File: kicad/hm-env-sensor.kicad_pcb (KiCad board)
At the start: 2 copper layers, 40 x 79 mm, 65 parts, among them Q1 Q12MHz/20pF/10ppm/4P/3.2x2.5mm, Q2 BC817-40(SOT23), Q3 BC817-40(SOT23), U1 BL4054B-42TPRN(SOT23-5), U2 CH340T(SSOP20W), U3 SY8089AAAC(SOT23-5), U4 BAT54C(SOT23-3), U5 ESP-WROOM-32, U6 BQ27441-G1, U7 BME280

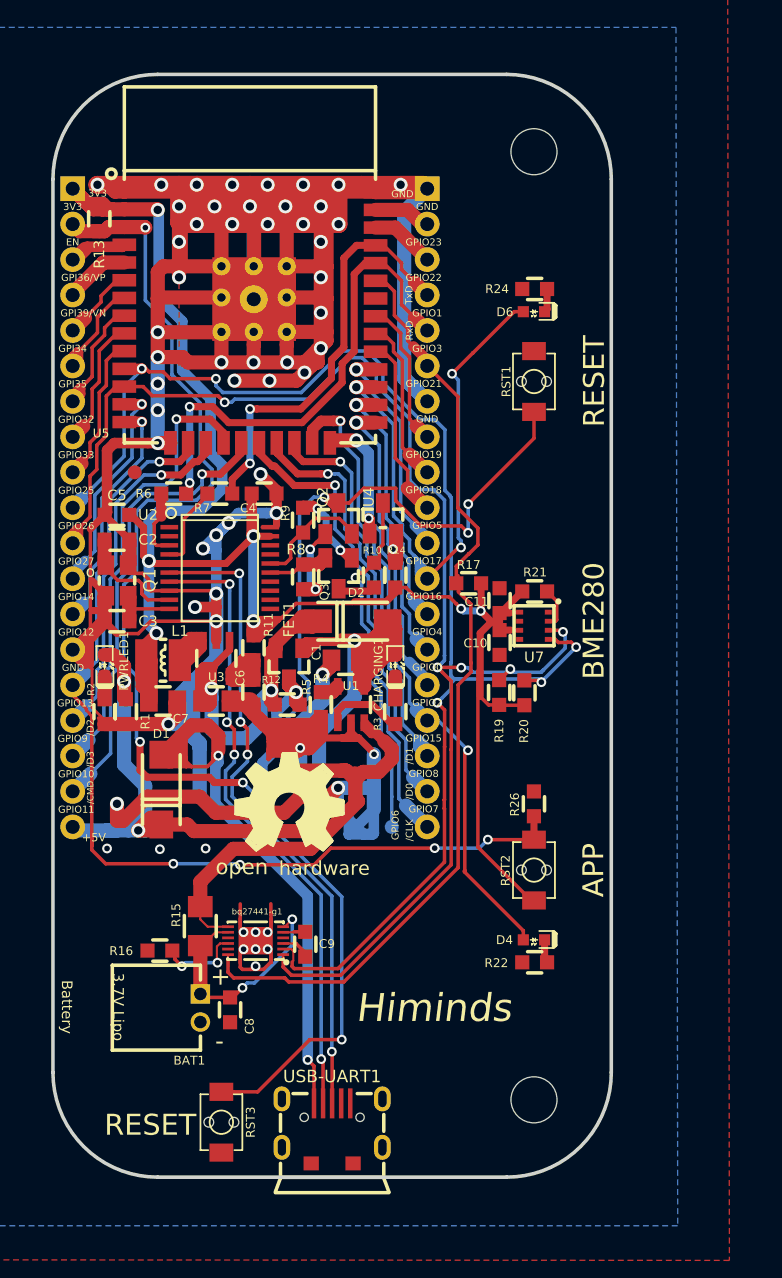
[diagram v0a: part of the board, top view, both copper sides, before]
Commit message: replace symbols and footrints by KiCAD libs + simplifiy schematic
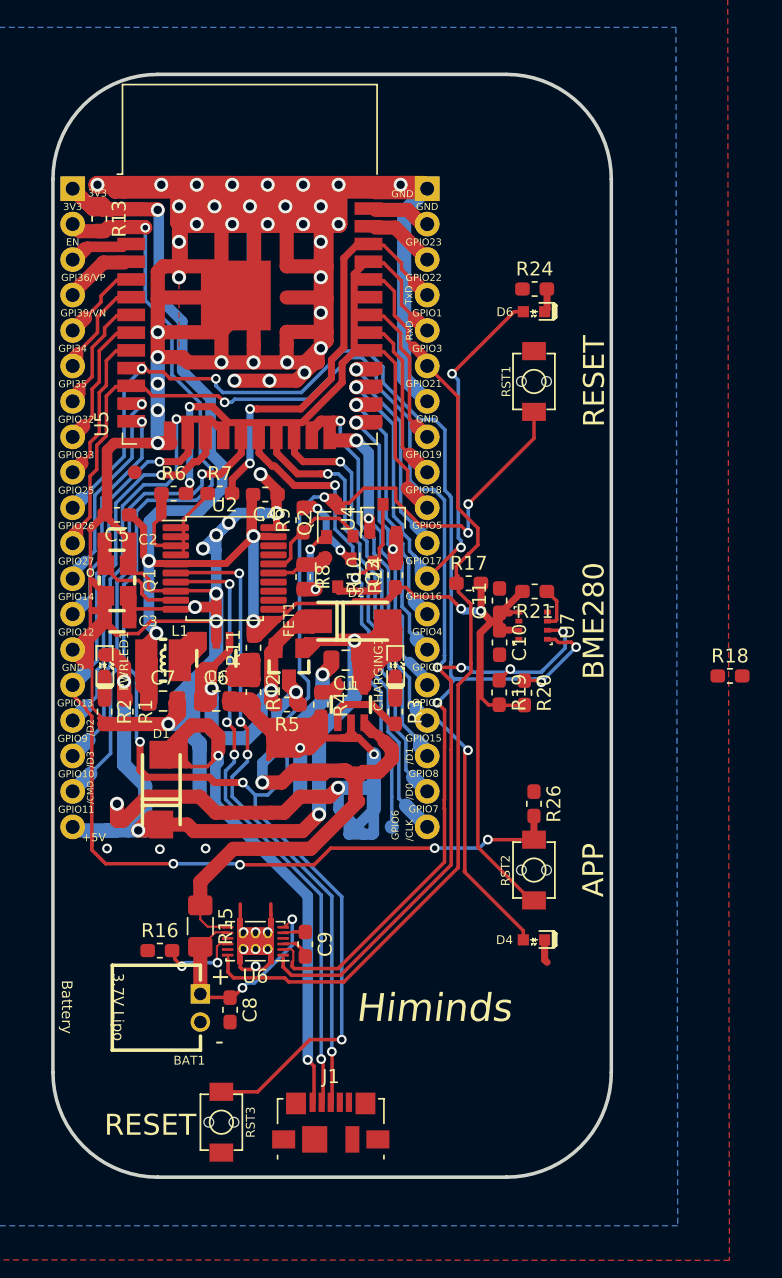
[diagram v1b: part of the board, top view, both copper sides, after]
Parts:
- removed ?: , OLIMEX_LOGOs-FP:LOGO_OPENHARDWARE_8x8
- removed MountingHole* (x2): Mounting_hole_3.3mm, OLIMEX_Other-FP:Mounting_hole_3.3mm
- removed R22: 330/R0603, OLIMEX_RLC-FP:R_0603_5MIL_DWS
- removed USB-UART1: MISB-SWMM-5B-LF(USB_MICRO), OLIMEX_Connectors-FP:USB-MICRO_MISB-SWMM-5B_LF
- added J1: USB_B_Micro, Connector_USB:USB_Micro-B_Molex_47346-0001, F.Cu at (149.3, 139.3)
- added R18: 330, Resistor_SMD:R_0603_1608Metric_Pad1.05x0.95mm_HandSolder, F.Cu at (177.9, 107.3)
- C1, C6, C7: value 47uF/6.3V/20%/X5R/C0805 -> 47u/6.3V; footprint OLIMEX_RLC-FP:C_0805_5MIL_DWS -> Capacitor_SMD:C_0805_2012Metric_Pad1.15x1.40mm_HandSolder
- C10, C11, C5: value 100nF/50V/20%/Y5V/C0603 -> 100n/50V; footprint OLIMEX_RLC-FP:C_0603_5MIL_DWS -> Capacitor_SMD:C_0603_1608Metric_Pad1.05x0.95mm_HandSolder
- C4: value 22uF/6.3V/20%/X5R/C0603 -> 22u/6.3V; footprint OLIMEX_RLC-FP:C_0603_5MIL_DWS -> Capacitor_SMD:C_0603_1608Metric_Pad1.05x0.95mm_HandSolder
- C8: value 1.0uF/16V/10%/Y5V/C0603 -> 1u/16V; footprint OLIMEX_RLC-FP:C_0603_5MIL_DWS -> Capacitor_SMD:C_0603_1608Metric_Pad1.05x0.95mm_HandSolder
- C9: value 0.47uF/50V/20%/Y5V/C0603 -> 470n/50V; footprint OLIMEX_RLC-FP:C_0603_5MIL_DWS -> Capacitor_SMD:C_0603_1608Metric_Pad1.05x0.95mm_HandSolder
- Q2, Q3: value BC817-40(SOT23) -> BC817; footprint OLIMEX_Transistors-FP:SOT23 -> Package_TO_SOT_SMD:SOT-23
- R1, R16, R26: value 10k/R0603 -> 10k; footprint OLIMEX_RLC-FP:R_0603_5MIL_DWS -> Resistor_SMD:R_0603_1608Metric_Pad1.05x0.95mm_HandSolder
- R10, R6, R7: value 220R/R0603 -> 220; footprint OLIMEX_RLC-FP:R_0603_5MIL_DWS -> Resistor_SMD:R_0603_1608Metric_Pad1.05x0.95mm_HandSolder
- R11: value 4.99k/1%/R0603 -> 4.99k/1%; footprint OLIMEX_RLC-FP:R_0603_5MIL_DWS -> Resistor_SMD:R_0603_1608Metric_Pad1.05x0.95mm_HandSolder
- R12: value 1.1k/1%/R0603 -> 1.1k; footprint OLIMEX_RLC-FP:R_0603_5MIL_DWS -> Resistor_SMD:R_0603_1608Metric_Pad1.05x0.95mm_HandSolder
- R13, R8, R9: value 1k/R0603 -> 1k; footprint OLIMEX_RLC-FP:R_0603_5MIL_DWS -> Resistor_SMD:R_0603_1608Metric_Pad1.05x0.95mm_HandSolder
- R14, R5: value NA/R0603 -> NA; footprint OLIMEX_RLC-FP:R_0603_5MIL_DWS -> Resistor_SMD:R_0603_1608Metric_Pad1.05x0.95mm_HandSolder
- R15: value 0.01/1%/R1206 -> 0.01/1%; footprint OLIMEX_RLC-FP:R_1206_5MIL_DWS -> Resistor_SMD:R_1206_3216Metric_Pad1.42x1.75mm_HandSolder
- R17, R19, R20, R21: value 4.7k/R0603 -> 4.7k; footprint OLIMEX_RLC-FP:R_0603_5MIL_DWS -> Resistor_SMD:R_0603_1608Metric_Pad1.05x0.95mm_HandSolder
- R2: value 2.2k/R0603 -> 10k; footprint OLIMEX_RLC-FP:R_0603_5MIL_DWS -> Resistor_SMD:R_0603_1608Metric_Pad1.05x0.95mm_HandSolder
- R24: value 330/R0603 -> 330; footprint OLIMEX_RLC-FP:R_0603_5MIL_DWS -> Resistor_SMD:R_0603_1608Metric_Pad1.05x0.95mm_HandSolder
- R3, R4: value 2.2k/R0603 -> 2.2k; footprint OLIMEX_RLC-FP:R_0603_5MIL_DWS -> Resistor_SMD:R_0603_1608Metric_Pad1.05x0.95mm_HandSolder
- U2: value CH340T(SSOP20W) -> CH340T; footprint OLIMEX_IC-FP:SSOP-20W -> Package_SO:SSOP-20_5.3x7.2mm_P0.65mm
- U4: value BAT54C(SOT23-3) -> BAT54A; footprint OLIMEX_Diodes-FP:SOT23-3 -> Package_TO_SOT_SMD:SOT-23
- U5: value ESP-WROOM-32 -> ESP32-WROOM-32; footprint OLIMEX_Cases-FP:ESP-WROOM-32_MODULE -> RF_Module:ESP32-WROOM-32
- U6: footprint sparkfun-battery-babysitter:PDSO-N12 -> Package_SON:Texas_S-PDSO-N12
- U7: footprint SparkFun_BME280_Breakout_v10:BME280_LGA -> Package_LGA:Bosch_LGA-8_2.5x2.5mm_P0.65mm_ClockwisePinNumbering
- moved U5 2.95 mm to (143.5, 80.8)
- moved U2 0.35 mm to (141.7, 99.6), turned to 0 degrees
- moved Q2 0.30 mm to (149.9, 96.3), turned to 90 degrees
- moved C4 0.11 mm to (144.6, 94.3), turned to 180 degrees
- moved Q3 0.08 mm to (149.8, 99.9), turned to 270 degrees
- moved U7 0.06 mm to (163.8, 103.7), turned to 270 degrees
- turned U6 to 180 degrees
- turned U4 to 90 degrees
- turned R14 to 90 degrees
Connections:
- C9 pad 1: Net-(C9-Pad1) -> GND
- C9 pad 2: GND -> Net-(C9-Pad2)
- R1 pad 1: +5V -> GND
- R1 pad 2: GND -> +5V
- R10 pad 1: Net-(Q3-Pad3) -> /D_Com
- R10 pad 2: /D_Com -> Net-(Q3-Pad3)
- R14 pad 1: /GPIO0 -> +3V3
- R14 pad 2: +3V3 -> /GPIO0
- R16 pad 1: GND -> Net-(R16-Pad1)
- R16 pad 2: Net-(R16-Pad2) -> GND
- R17 pad 1: /GPIO21 -> +3V3
- R17 pad 2: +3V3 -> /GPIO21
- R19 pad 1: /GPIO27 -> +3V3
- R19 pad 2: +3V3 -> /GPIO27
- R2 pad 1: Net-(PWRLED1-Pad1) -> GND
- R2 pad 2: GND -> Net-(PWRLED1-Pad1)
- R20 pad 1: /GPIO26 -> +3V3
- R20 pad 2: +3V3 -> /GPIO26
- R21 pad 1: Net-(R21-Pad1) -> +3V3
- R21 pad 2: +3V3 -> Net-(R21-Pad2)
- R24 pad 1: GND -> Net-(D6-Pad1)
- R24 pad 2: Net-(D6-Pad1) -> GND
- R26 pad 1: GND -> /GPIO13
- R26 pad 2: /GPIO13 -> GND
- R6 pad 1: Net-(R6-Pad1) -> /GPIO3/U0RXD
- R6 pad 2: /GPIO3/U0RXD -> Net-(R6-Pad2)
- R7 pad 1: Net-(R7-Pad1) -> /GPIO1/U0TXD
- R7 pad 2: /GPIO1/U0TXD -> Net-(R7-Pad2)
- R8 pad 1: Net-(Q3-Pad2) -> Net-(Q2-Pad1)
- R8 pad 2: Net-(Q2-Pad1) -> Net-(Q3-Pad2)
- R9 pad 1: Net-(Q2-Pad2) -> Net-(Q3-Pad1)
- R9 pad 2: Net-(Q3-Pad1) -> Net-(Q2-Pad2)
- U2 pad 1: (no net) -> Net-(U2-Pad1)
- U2 pad 18: (no net) -> Net-(U2-Pad18)
- U2 pad 2: (no net) -> Net-(U2-Pad2)
- U2 pad 3: Net-(R6-Pad1) -> Net-(R6-Pad2)
- U2 pad 4: Net-(R7-Pad1) -> Net-(R7-Pad2)
- U5 pad 4: /GPI36/SENSOR_VP -> Net-(U5-Pad4)
- U5 pad 5: /GPI39/SENSOR_VN -> Net-(U5-Pad5)
- U6 pad 10: Net-(R16-Pad2) -> Net-(R16-Pad1)
- U6 pad 11: (no net) -> Net-(U6-Pad11)
- U6 pad 4: (no net) -> Net-(U6-Pad4)
- U6 pad 5: Net-(C9-Pad1) -> Net-(C9-Pad2)
- U6 pad 9: (no net) -> Net-(U6-Pad9)

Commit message: aktuell
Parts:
- removed D_Com1, GND1: TESTPAD, OLIMEX_Other-FP:TESTPAD_40-ROUND
- removed EXT1, EXT2: HN1x19, OLIMEX_Connectors-FP:HN1x19
- removed FET1: WPM2015-3/TR, OLIMEX_Transistors-FP:SOT23
- removed J1: USB_B_Micro, Connector_USB:USB_Micro-B_Molex_47346-0001
- removed Q1: Q12MHz/20pF/10ppm/4P/3.2x2.5mm, OLIMEX_Crystal-FP:TSX-3.2x2.5mm_GND(3)
- removed RST1: IT-1185AU2-160G-G-TR, OLIMEX_Buttons-FP:IT1185AU2_V2
- removed U4: BAT54A, Package_TO_SOT_SMD:SOT-23
- added C12: 100p/6.3V, Capacitor_SMD:C_0805_2012Metric_Pad1.15x1.40mm_HandSolder, F.Cu at (209.5, 96.0)
- added D3: BAT54C, Package_TO_SOT_SMD:SOT-23, F.Cu at (163.4, 97.2)
- added FID1: Fiducial, Fiducial:Fiducial_1mm_Mask2mm, F.Cu at (197.1, 115.8)
- added FID2: Fiducial, Fiducial:Fiducial_1mm_Mask2mm, F.Cu at (218.7, 91.8)
- added H1: MountingHole, MountingHole:MountingHole_3.2mm_M3, F.Cu at (165.4, 74.7)
- added H2: MountingHole, MountingHole:MountingHole_3.2mm_M3, F.Cu at (133.4, 74.7)
- added H3: MountingHole, MountingHole:MountingHole_3.2mm_M3, F.Cu at (133.4, 133.7)
- added H4: MountingHole, MountingHole:MountingHole_3.2mm_M3, F.Cu at (165.4, 133.7)
- added J2: Conn_01x06_Female, Connector_PinSocket_2.54mm:PinSocket_1x06_P2.54mm_Vertical, F.Cu at (185.7, 68.8)
- added P1: USB_C_Plug_USB2.0, Connector_USB:USB_C_Receptacle_Amphenol_12401548E4-2A, F.Cu at (155.4, 137.7)
- added Q4: NTR4101PT1G, Package_TO_SOT_SMD:SOT-23, F.Cu at (193.1, 116.2)
- added R22: 10k, Resistor_SMD:R_0603_1608Metric_Pad1.05x0.95mm_HandSolder, F.Cu at (226.3, 68.8)
- added R23: dnp, Resistor_SMD:R_0603_1608Metric_Pad1.05x0.95mm_HandSolder, F.Cu at (226.3, 71.3)
- added R25: dnp, Resistor_SMD:R_0603_1608Metric_Pad1.05x0.95mm_HandSolder, F.Cu at (230.6, 68.8)
- added R27: 10k, Resistor_SMD:R_0603_1608Metric_Pad1.05x0.95mm_HandSolder, F.Cu at (230.6, 71.3)
- added TP1: D_Com1, TestPoint:TestPoint_THTPad_D2.0mm_Drill1.0mm, F.Cu at (206.4, 107.6)
- added TP2: GND, TestPoint:TestPoint_THTPad_D2.0mm_Drill1.0mm, F.Cu at (213.6, 99.8)
- added TP3: 5V, TestPoint:TestPoint_THTPad_D2.0mm_Drill1.0mm, F.Cu at (218.2, 97.3)
- added TP4: 3.3V, TestPoint:TestPoint_THTPad_D2.0mm_Drill1.0mm, F.Cu at (213.5, 104.0)
- added Y1: 12 MHz, Crystal:Crystal_SMD_HC49-SD_HandSoldering, F.Cu at (152.9, 107.2)
- BAT1: value DW02S -> Conn_01x02_Male; footprint OLIMEX_Connectors-FP:LIPO_BAT-CON2DW02R -> Connector_JST:JST_PH_S2B-PH-K_1x02_P2.00mm_Horizontal
- C2, C3: value 27pF/50V/5%/C0G/C0603 -> 22p/50V/C0G; footprint OLIMEX_RLC-FP:C_0603_5MIL_DWS -> Capacitor_SMD:C_0603_1608Metric_Pad1.05x0.95mm_HandSolder
- C6, C7: value 47u/6.3V -> 10u/6.3V
- CHARGING1: value LED/YELLOW/0603 -> LED/Yellow; footprint OLIMEX_LEDs-FP:LED_0603_KA -> LED_SMD:LED_0603_1608Metric_Pad1.05x0.95mm_HandSolder
- D1, D2: value 1N5822/SS34/SMA -> 1N5822; footprint OLIMEX_Diodes-FP:SMA-KA -> Diode_SMD:D_SMC_Handsoldering
- D4: value LED/GREEN/0603 -> LED/Green; footprint OLIMEX_LEDs-FP:LED_0603_KA -> LED_SMD:LED_0603_1608Metric_Pad1.05x0.95mm_HandSolder
- D6: value LED/RED/0603 -> LED/Blue; footprint OLIMEX_LEDs-FP:LED_0603_KA -> LED_SMD:LED_0603_1608Metric_Pad1.05x0.95mm_HandSolder
- FID3: footprint OLIMEX_Other-FP:Fiducial1x3 -> Fiducial:Fiducial_1mm_Mask2mm
- L1: value 2.2uH/1.5A/DCR<0.1R/CD32 -> 4.7u; footprint OLIMEX_RLC-FP:CD32 -> Inductor_SMD:L_Wuerth_WE-TPC-3816
- PWRLED1: value LED/RED/0603 -> LED/Red; footprint OLIMEX_LEDs-FP:LED_0603_KA -> LED_SMD:LED_0603_1608Metric_Pad1.05x0.95mm_HandSolder
- R11: value 4.99k/1% -> 540k
- R12: value 1.1k -> 120k
- RST2, RST3: value IT-1185AU2-160G-G-TR -> SW_Push; footprint OLIMEX_Buttons-FP:IT1185AU2_V2 -> Button_Switch_SMD:SW_SPST_PTS645
- U1: value BL4054B-42TPRN(SOT23-5) -> LTC4054ES5-4.2; footprint OLIMEX_IC-FP:SOT-23-5 -> Package_TO_SOT_SMD:TSOT-23-5
- U3: value SY8089AAAC(SOT23-5) -> PAM2305AABADJ; footprint OLIMEX_Regulators-FP:SOT-23-5 -> Package_TO_SOT_SMD:TSOT-23-5
- moved D2 99.6 mm to (52.9, 121.2)
- moved FID3 82.5 mm to (217.4, 101.1)
- moved RST3 75.6 mm to (202.0, 93.9), turned to 0 degrees
- moved U3 70.1 mm to (209.8, 92.3), turned to 0 degrees
- moved R24 67.9 mm to (231.4, 86.7)
- moved CHARGING1 62.7 mm to (214.7, 91.3), turned to 0 degrees
- moved D4 60.2 mm to (214.7, 93.9), turned to 0 degrees
- moved L1 54.4 mm to (191.7, 108.5), turned to 0 degrees
- moved D6 50.5 mm to (209.3, 103.3), turned to 0 degrees
- moved D1 47.1 mm to (95.9, 138.2), turned to 180 degrees
- moved U1 46.6 mm to (197.3, 107.8), turned to 0 degrees
- moved PWRLED1 44.3 mm to (164.0, 138.2), turned to 0 degrees
- moved R1 43.6 mm to (166.9, 139.2), turned to 90 degrees
- moved R2 43.2 mm to (163.9, 140.2), turned to 180 degrees
- moved RST2 42.9 mm to (202.0, 101.7), turned to 0 degrees
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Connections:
- net /GPIO21 renamed /BAT_LOW
- C9 pad 1: GND -> Net-(C9-Pad1)
- C9 pad 2: Net-(C9-Pad2) -> GND
- D4 pad 2: /GPIO15 -> /USER_LED_Green
- D6 pad 2: /GPIO16 -> /USER_LED_Blue
- R11 pad 1: Net-(R11-Pad1) -> Net-(C12-Pad2)
- R12 pad 1: Net-(R11-Pad1) -> Net-(C12-Pad2)
- R19 pad 2: /GPIO27 -> /SCL
- R20 pad 2: /GPIO26 -> /SDA
- RST2 pad 1: +3V3 -> /GPIO13
- RST2 pad 2: /GPIO13 -> +3V3
- RST3 pad 1: /ESP_EN -> GND
- RST3 pad 2: GND -> /ESP_EN
- U2 pad 1: Net-(U2-Pad1) -> (no net)
- U2 pad 11: Net-(U2-Pad11) -> (no net)
- U2 pad 12: Net-(U2-Pad12) -> (no net)
- U2 pad 13: Net-(U2-Pad13) -> (no net)
- U2 pad 14: Net-(U2-Pad14) -> (no net)
- U2 pad 17: Net-(U2-Pad17) -> (no net)
- U2 pad 18: Net-(U2-Pad18) -> (no net)
- U2 pad 2: Net-(U2-Pad2) -> (no net)
- U3 pad 3: Net-(L1-Pad1) -> Net-(C6-Pad1)
- U3 pad 4: Net-(C6-Pad1) -> Net-(C12-Pad2)
- U3 pad 5: Net-(R11-Pad1) -> Net-(L1-Pad1)
- U5 pad 10: /GPIO25 -> (no net)
- U5 pad 11: /GPIO26 -> /SCL
- U5 pad 12: /GPIO27 -> /SDA
- U5 pad 13: /GPIO14 -> (no net)
- U5 pad 14: /GPIO12 -> (no net)
- U5 pad 16: /GPIO13 -> (no net)
- U5 pad 17: /GPIO9/SD_DATA2 -> (no net)
- U5 pad 18: /GPIO10/SD_DATA3 -> (no net)
- U5 pad 19: /GPIO11/SD_CMD -> (no net)
- U5 pad 20: /GPIO6/SD_CLK -> (no net)
- U5 pad 21: /GPIO7/SD_DATA0 -> (no net)
- U5 pad 22: /GPIO8/SD_DATA1 -> (no net)
- U5 pad 23: /GPIO15 -> (no net)
- U5 pad 26: /GPIO4 -> (no net)
- U5 pad 27: /GPIO16 -> /USER_LED_Green
- U5 pad 28: /GPIO17 -> /USER_LED_Blue
- U5 pad 29: /GPIO5 -> (no net)
- U5 pad 30: /GPIO18 -> (no net)
- U5 pad 31: /GPIO19 -> (no net)
- U5 pad 32: Net-(U5-Pad32) -> (no net)
- U5 pad 36: /GPIO22 -> (no net)
- U5 pad 37: /GPIO23 -> (no net)
- U5 pad 4: Net-(U5-Pad4) -> (no net)
- U5 pad 5: Net-(U5-Pad5) -> (no net)
- U5 pad 6: /GPI34 -> (no net)
- U5 pad 7: /GPI35 -> (no net)
- U5 pad 8: /GPIO32 -> (no net)
- U5 pad 9: /GPIO33 -> (no net)
- U6 pad 1: /GPIO27 -> /SDA
- U6 pad 2: /GPIO26 -> /SCL
- U6 pad 5: Net-(C9-Pad2) -> Net-(C9-Pad1)
- U7 pad 3: /GPIO27 -> /SCL
- U7 pad 4: /GPIO26 -> /SDA
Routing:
- net GND: track 438.5 -> 6.21 mm, vias 59 -> 0
- net +3V3: track 146.7 -> 0.00 mm, vias 7 -> 0
- net /ESP_EN: track 142.0 -> 0.00 mm, vias 7 -> 0
- net /GPIO27: track 104.0 -> 0.00 mm, vias 5 -> 0
- net /GPIO26: track 103.2 -> 0.00 mm, vias 5 -> 0
- net +5V: track 93.3 -> 0.00 mm, vias 4 -> 0
- net /GPIO13: track 69.7 -> 0.00 mm, vias 5 -> 0
- net /BAT_LOW: track 69.4 -> 0.00 mm
- net V_BATT: track 53.4 -> 2.31 mm, vias 2 -> 0
- net /GPIO16: track 47.4 -> 0.00 mm, vias 3 -> 0
- net Net-(P1-PadA6): track 47.1 -> 0.00 mm, vias 4 -> 0
- net /GPIO15: track 46.5 -> 0.00 mm, vias 2 -> 0
- net /+5V_USB: track 46.3 -> 0.00 mm, vias 2 -> 0
- net Net-(P1-PadA7): track 45.1 -> 0.00 mm, vias 4 -> 0
- net /GPIO3/U0RXD: track 35.6 -> 0.00 mm, vias 2 -> 0
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- removed copper zone on B.Cu, net GND
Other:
- net class Default: clearance 0.223 -> 0.2; trace_width 0.254 -> 0.2
- rule trace_clearance: 0.223 -> 0.2
- board text removed: "+5V"
- board text removed: "/CLK"
- board text removed: "/CMD"
- board text removed: "/D0"
- board text removed: "/D1"
- board text removed: "/D2"
- board text removed: "/D3"
- board text removed: "3.7V Lipo Battery"
- board text removed: "3V3"
- board text removed: "APP"
- board text removed: "BME280"
- board text removed: "EN"
- board text removed: "ESP_EN"
- board text removed: "GND"
- board text removed: "GPI34"
- board text removed: "GPI35"
- board text removed: "GPI36/VP"
- board text removed: "GPI39/VN"
- board text removed: "GPIO1"
- board text removed: "GPIO1/ U0TXD"
- board text removed: "GPIO10"
- board text removed: "GPIO10/ SD_DATA3"
- board text removed: "GPIO11"
- board text removed: "GPIO11/ SD_CMD"
- board text removed: "GPIO12"
- board text removed: "GPIO13"
- board text removed: "GPIO14"
- board text removed: "GPIO18"
- board text removed: "GPIO19"
- board text removed: "GPIO21"
- board text removed: "GPIO22"
- board text removed: "GPIO23"
- board text removed: "GPIO25"
- board text removed: "GPIO26"
- board text removed: "GPIO27"
- board text removed: "GPIO3"
- board text removed: "GPIO3/ U0RXD"
- board text removed: "GPIO32"
- board text removed: "GPIO33"
- board text removed: "GPIO6"
- board text removed: "GPIO6/ SD_CLK"
- board text removed: "GPIO7"
- board text removed: "GPIO7/ SD_DATA0"
- board text removed: "GPIO8"
- board text removed: "GPIO8/ SD_DATA1"
- board text removed: "GPIO9"
- board text removed: "GPIO9/ SD_DATA2"
- board text removed: "Himinds"
- board text removed: "RESET"
- board text removed: "RxD"
- board text removed: "TxD"
- board text removed: "https://github.com/himinds"
- board text removed: "hw-env-sensor Rev.A"
